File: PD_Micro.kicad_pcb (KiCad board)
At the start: 2 copper layers, 62 x 53 mm, 43 parts, among them J1 Conn_01x02, Q1 DMP3017SFK, Q2 DTC143E, SW1 SW_DIP_x06, SW2 SW_DPST_x2, SW3 SW_Push, SW4 SW_Push, SW5 SW_DPST_x2, U1 SRV05-4, U2 Pico, U3 TPS62175DQC, U4 FUSB302BMPX, U5 ACS723xMATR-10AB, U6 oledSym

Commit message: pcb
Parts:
- SW2: renamed from SW4; footprint Button_Switch_SMD:SW_SPST_TL3305C -> Button_Switch_SMD:SW_SPST_TL3305B
- SW6: renamed from SW3; footprint Button_Switch_SMD:SW_SPST_TL3305C -> Button_Switch_SMD:SW_SPST_TL3305B
- moved SW4 2.83 mm to (220.5, 137.9)
- moved SW1 2.79 mm to (210.7, 137.8)
- moved SW6 0.13 mm to (230.9, 126.4)
- renumbered C11 to C1, C1 to C12, C9 to C13, C12 to C15, C6 to C16, C4 to C17, C8 to C2, C10 to C3, C7 to C4, C2 to C6, C3 to C7, C5 to C8, H2 to H1, H4 to H2, H1 to H3, H3 to H4, J1 to J3, R5 to R1, R9 to R11, R8 to R12, R4 to R2, R6 to R3, R7 to R4, R2 to R7, R1 to R8, R3 to R9, SW2 to SW1, SW5 to SW4, SW1 to SW5, U3 to U1, U1 to U2, U2 to U3
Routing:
- net Net-(SW1A-B): track 42.7 -> 45.8 mm
- net Net-(SW4A-B): track 24.5 -> 27.3 mm

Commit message: silk
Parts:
- added G***: LOGO, LOGO, F.Cu at (233.3, 110.5)
- added G***: LOGO, LOGO, B.Cu at (213.9, 114.9)
- added G***: LOGO, LOGO, B.Cu at (203.5, 132.3)
- added G***: LOGO, LOGO, B.Cu at (180.1, 130.1)
- added G***: LOGO, LOGO, B.Cu at (183.3, 135.8)
- added G***: LOGO, LOGO, B.Cu at (225.4, 115.2)
- added G***: LOGO, LOGO, B.Cu at (193.7, 134.7)
- added G***: LOGO, LOGO, B.Cu at (180.1, 121.0)
- added G***: LOGO, LOGO, B.Cu at (229.4, 93.0)
- added G***: LOGO, LOGO, B.Cu at (219.3, 133.0)
- added G***: LOGO, LOGO, B.Cu at (220.9, 103.3)
- added G***: LOGO, LOGO, B.Cu at (201.6, 119.4)
- added G***: LOGO, LOGO, B.Cu at (230.3, 121.2)
- added G***: LOGO, LOGO, B.Cu at (207.0, 101.2)
- added G***: LOGO, LOGO, B.Cu at (191.7, 122.6)
- renumbered C12 to C1, C13 to C10, C1 to C11, C15 to C12, C6 to C2, C16 to C3, C8 to C4, C17 to C5, C7 to C6, C4 to C7, C3 to C8, C2 to C9, H3 to H1, H1 to H2, H4 to H3, H2 to H4, J3 to J1, R9 to R1, R8 to R2, R7 to R3, R12 to R4, R4 to R5, R1 to R6, R2 to R7, R3 to R8, R11 to R9, SW5 to SW1, SW1 to SW2, SW6 to SW3, SW2 to SW4, SW4 to SW5, U2 to U1, U3 to U2, U1 to U3
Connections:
- U2 pad 33: unconnected-(U3-AGND-Pad33) -> GND
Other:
- board text added: "HTL-Rankweil 4AHEL Manuel Mayrhofer Johannes Melcher-Millner USBC_PD-Trigger"

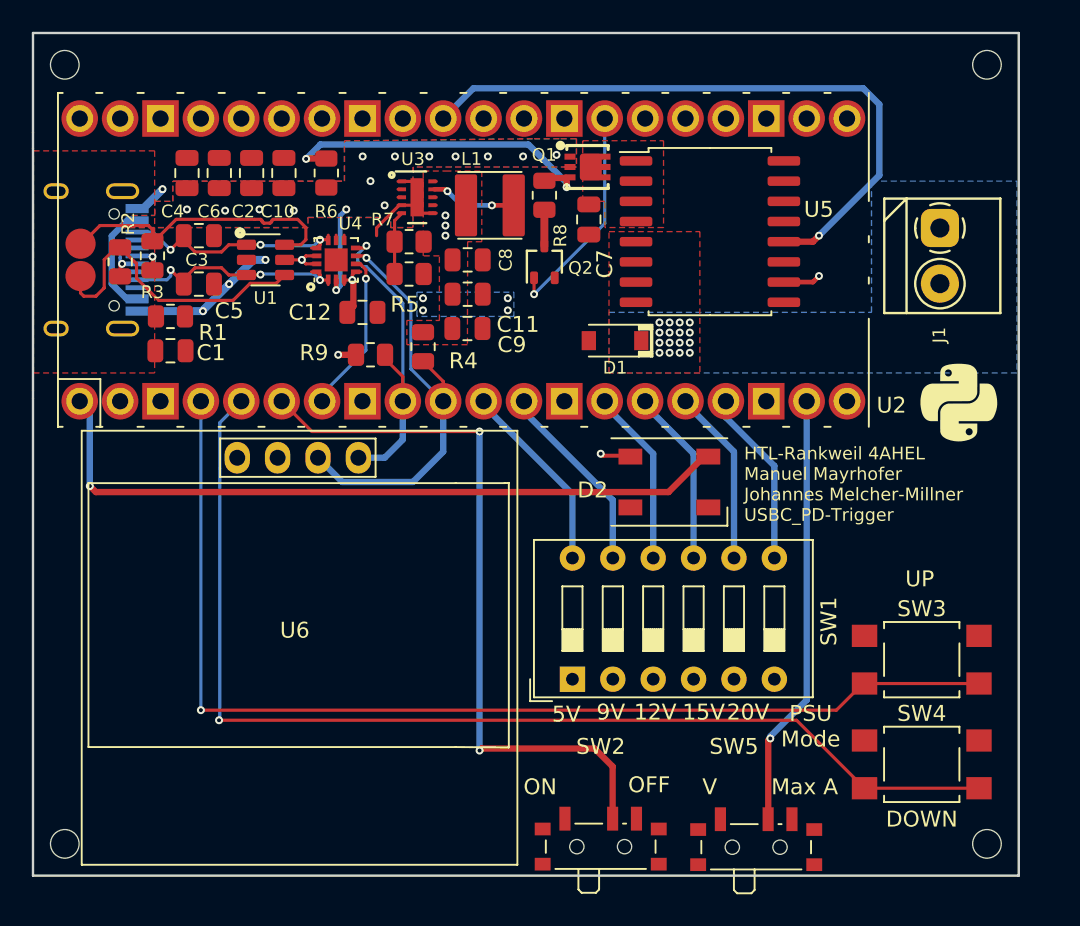
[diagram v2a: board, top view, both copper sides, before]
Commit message: bevore silkscreen delete
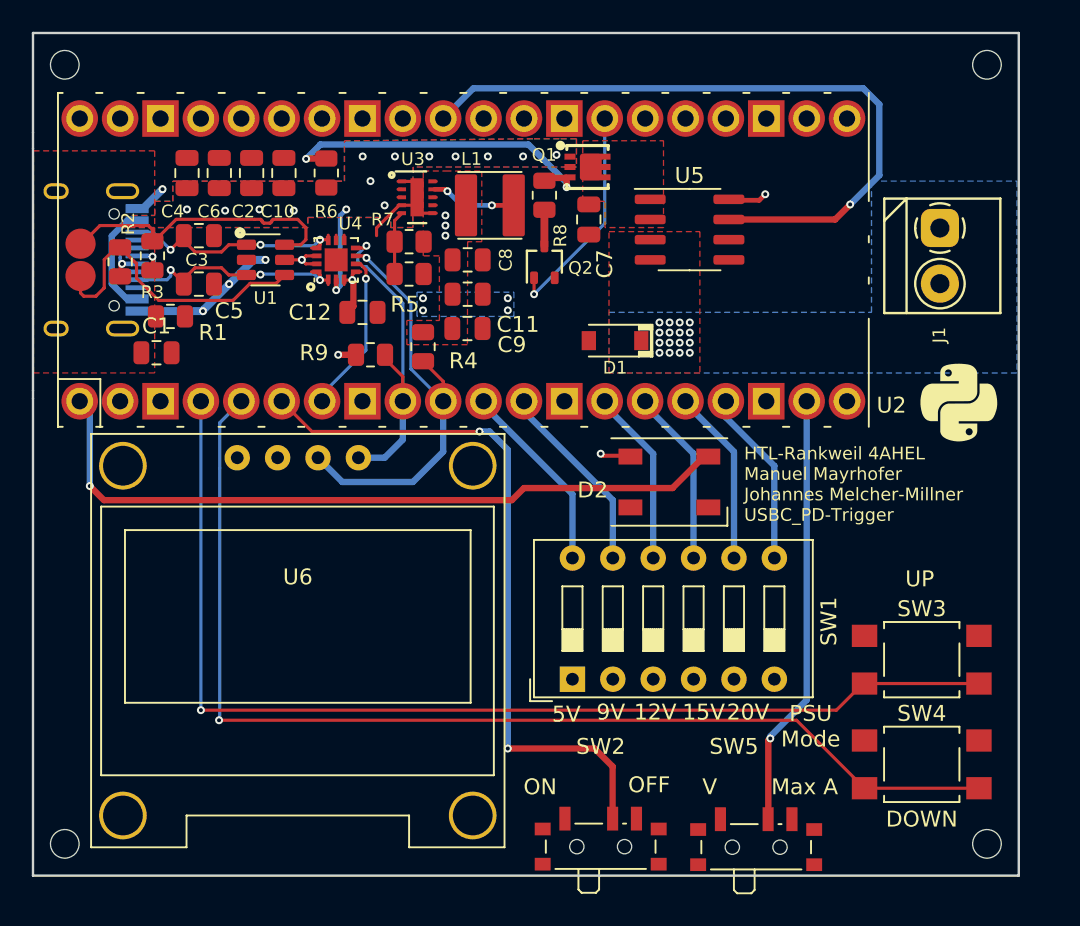
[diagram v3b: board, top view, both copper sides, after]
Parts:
- U5: value ACS723xMATR-10AB -> ACS723xLCTR-10AB; footprint Package_SO:SOIC-16W_7.5x10.3mm_P1.27mm -> Package_SO:SOIC-8_3.9x4.9mm_P1.27mm
- U6: footprint SSD1306:128x64OLED -> OLED094:SSD1306_0.96_Oled
- moved U6 18.9 mm to (178.7, 138.2)
- moved U5 1.29 mm to (216.3, 99.4)
- moved C1 0.89 mm to (182.8, 107.1)
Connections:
- U5 pad 3: /HALL_IN -> /OUT
- U5 pad 4: /HALL_IN -> /OUT
- U5 pad 5: /OUT -> GND
- U5 pad 6: /OUT -> GND
- U5 pad 7: /OUT -> ADC0
- U5 pad 8: /OUT -> +5V
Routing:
- net ADC0: track 40.8 -> 43.7 mm
- net Net-(SW2A-B): track 45.8 -> 44.9 mm

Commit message: v1 sent to zudrell
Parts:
- removed the G*** at (213.9, 114.9)
- removed the G*** at (203.5, 132.3)
- removed the G*** at (180.1, 130.1)
- removed the G*** at (183.3, 135.8)
- removed the G*** at (225.4, 115.2)
- removed the G*** at (193.7, 134.7)
- removed the G*** at (180.1, 121.0)
- removed the G*** at (229.4, 93.0)
- removed the G*** at (220.9, 103.3)
- removed the G*** at (201.6, 119.4)
- removed the G*** at (207.0, 101.2)
- removed the G*** at (191.7, 122.6)
- moved G*** 31.5 mm to (188.6, 125.9)
- moved G*** 23.5 mm to (206.9, 118.2)
